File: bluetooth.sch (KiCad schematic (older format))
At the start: 8 parts, among them SW2 SW_PUSH, U7 WT12-A

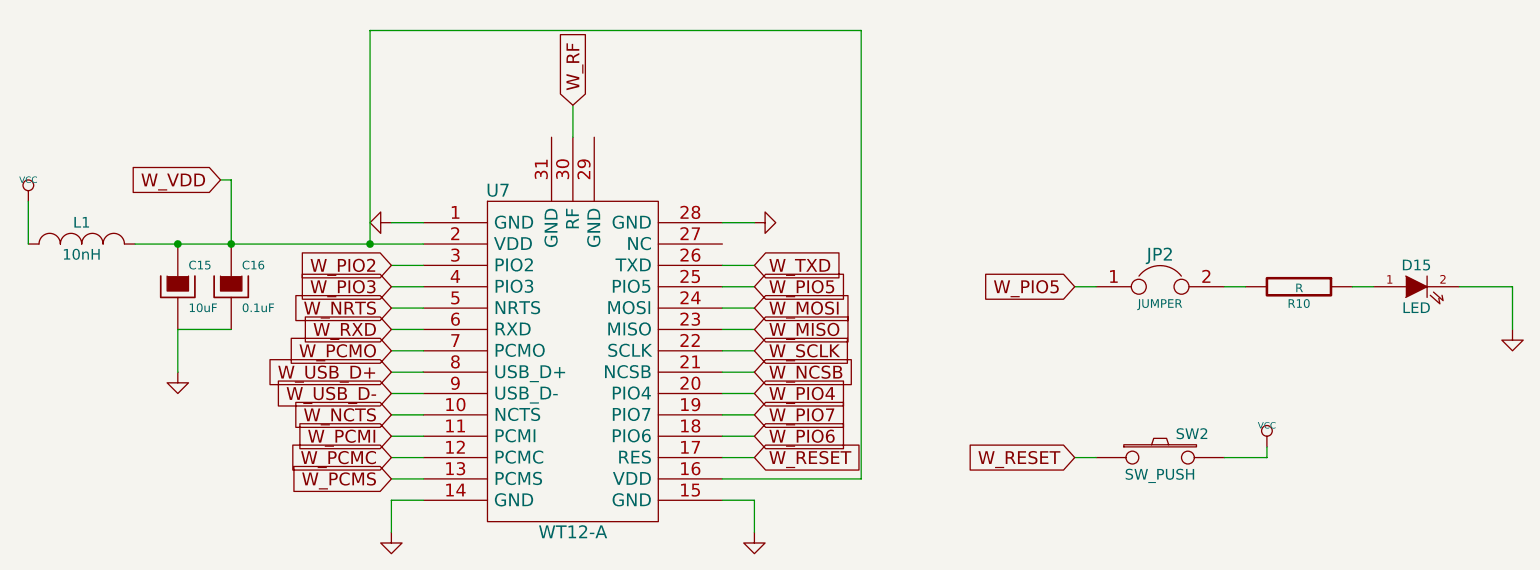
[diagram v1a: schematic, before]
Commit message: Remove most solder jumpers
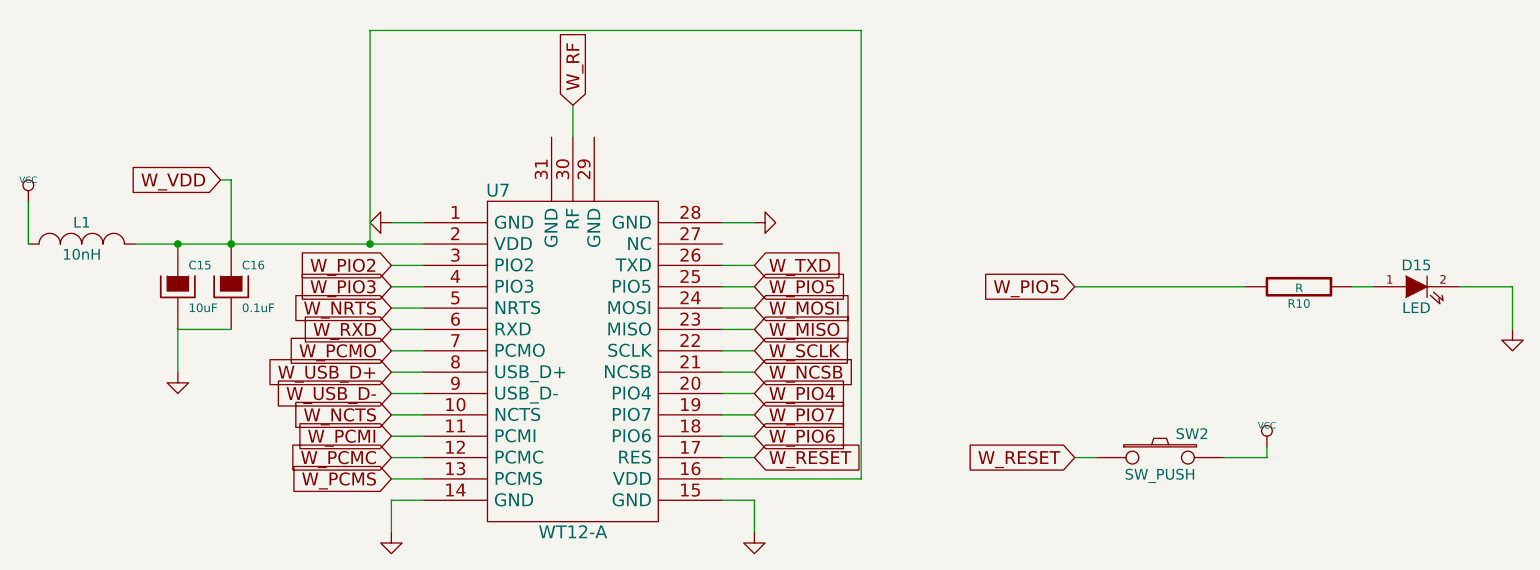
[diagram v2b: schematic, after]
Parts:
- removed JP2: JUMPER, replacement_kinesis_controller:JUMPER_2, symbol JUMPER
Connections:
- net W_PIO5: now also R10.2
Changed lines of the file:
@@
 W_RF
 $Comp
-L GND #PWR52
+L GND #PWR049
 U 1 1 54E5E1AE
 P 5050 4850
-F 0 "#PWR52" H 5050 4850 30  0001 C CNN
+F 0 "#PWR049" H 5050 4850 30  0001 C CNN
 F 1 "GND" H 5050 4780 30  0001 C CNN
 F 2 "" H 5050 4850 60  0000 C CNN
@@
 $EndComp
 $Comp
-L GND #PWR51
+L GND #PWR050
 U 1 1 54E5E1B4
 P 5050 3400
-F 0 "#PWR51" H 5050 3400 30  0001 C CNN
+F 0 "#PWR050" H 5050 3400 30  0001 C CNN
 F 1 "GND" H 5050 3330 30  0001 C CNN
 F 2 "" H 5050 3400 60  0000 C CNN
@@
 $EndComp
 $Comp
-L GND #PWR53
+L GND #PWR051
 U 1 1 54E5E1BA
 P 6750 3400
-F 0 "#PWR53" H 6750 3400 30  0001 C CNN
+F 0 "#PWR051" H 6750 3400 30  0001 C CNN
 F 1 "GND" H 6750 3330 30  0001 C CNN
 F 2 "" H 6750 3400 60  0000 C CNN
@@
 $EndComp
 $Comp
-L GND #PWR54
+L GND #PWR052
 U 1 1 54E5E1C0
 P 6750 4850
-F 0 "#PWR54" H 6750 4850 30  0001 C CNN
+F 0 "#PWR052" H 6750 4850 30  0001 C CNN
 F 1 "GND" H 6750 4780 30  0001 C CNN
 F 2 "" H 6750 4850 60  0000 C CNN
@@
 $EndComp
 $Comp
-L GND #PWR50
+L GND #PWR053
 U 1 1 54E5E1D4
 P 4050 4100
-F 0 "#PWR50" H 4050 4100 30  0001 C CNN
+F 0 "#PWR053" H 4050 4100 30  0001 C CNN
 F 1 "GND" H 4050 4030 30  0001 C CNN
 F 2 "" H 4050 4100 60  0000 C CNN
@@
 $EndComp
 $Comp
-L VCC #PWR49
+L VCC #PWR054
 U 1 1 54E5E1E1
 P 3350 3300
-F 0 "#PWR49" H 3350 3400 30  0001 C CNN
+F 0 "#PWR054" H 3350 3400 30  0001 C CNN
 F 1 "VCC" H 3350 3400 30  0000 C CNN
 F 2 "" H 3350 3300 60  0000 C CNN
@@
 W_RESET
 $Comp
-L VCC #PWR55
+L VCC #PWR055
 U 1 1 54E7230E
 P 9150 4450
-F 0 "#PWR55" H 9150 4550 30  0001 C CNN
+F 0 "#PWR055" H 9150 4550 30  0001 C CNN
 F 1 "VCC" H 9150 4550 30  0000 C CNN
 F 2 "" H 9150 4450 60  0000 C CNN
@@
 Text GLabel 8250 3700 0    60   Input ~ 0
 W_PIO5
-$Comp
-L JUMPER JP2
-U 1 1 54E9AF59
-P 8650 3700
-F 0 "JP2" H 8650 3850 60  0000 C CNN
-F 1 "JUMPER" H 8650 3620 40  0000 C CNN
-F 2 "replacement_kinesis_controller:JUMPER_2" H 8650 3700 60  0001 C CNN
-F 3 "" H 8650 3700 60  0000 C CNN
-	1    8650 3700
-	1    0    0    -1
-$EndComp
 $Comp
 L R R10
@@
 $EndComp
 $Comp
-L GND #PWR56
+L GND #PWR056
 U 1 1 54E9B03C
 P 10300 3900
-F 0 "#PWR56" H 10300 3900 30  0001 C CNN
+F 0 "#PWR056" H 10300 3900 30  0001 C CNN
 F 1 "GND" H 10300 3830 30  0001 C CNN
 F 2 "" H 10300 3900 60  0000 C CNN
@@
 	9650 3700 9550 3700
 Wire Wire Line
-	9050 3700 8950 3700
-Wire Wire Line
-	8350 3700 8250 3700
+	8250 3700 9050 3700
 Text GLabel 4250 3200 0    60   Input ~ 0
 W_VDD
